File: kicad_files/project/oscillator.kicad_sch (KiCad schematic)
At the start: 3 parts, among them X1 TXM12M0004252DBCEO00T

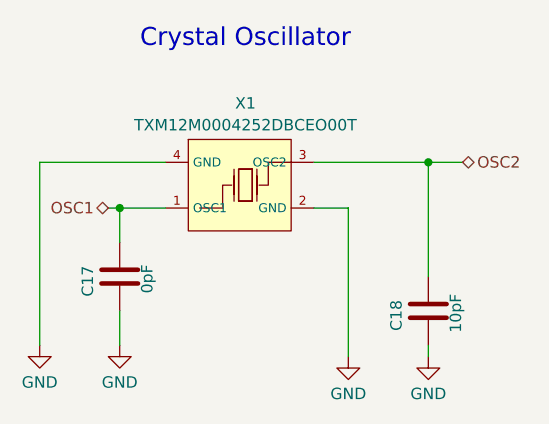
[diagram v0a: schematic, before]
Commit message: started with board layout, also added more stuff on the schematic
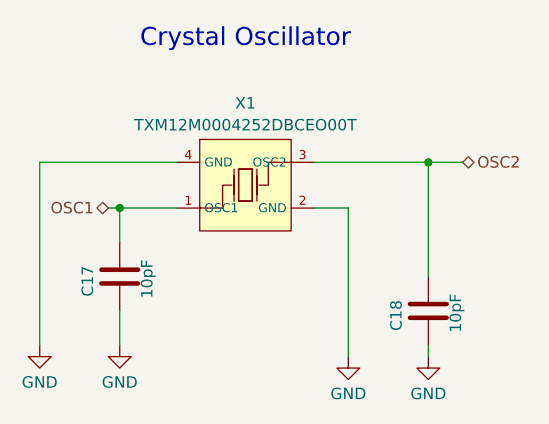
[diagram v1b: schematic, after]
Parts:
- C17: value 0pF -> 10pF
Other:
- moved on the sheet: X1
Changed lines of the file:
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@@
 	(wire
 		(pts
-			(xy 123.19 91.44) (xy 128.27 91.44)
+			(xy 123.19 91.44) (xy 129.54 91.44)
 		)
 		(stroke
@@
 	(wire
 		(pts
-			(xy 114.3 86.36) (xy 128.27 86.36)
+			(xy 114.3 86.36) (xy 129.54 86.36)
 		)
 		(stroke
@@
 		(dnp no)
 		(fields_autoplaced yes)
-		(property "Reference" "#PWR033"
+		(property "Reference" "#PWR044"
 			(at 123.19 113.03 0)
 			(effects
@@
 			(project "FABulous_board"
 				(path "/5664f05e-a3ef-4177-8026-c4580fa32c71/b4d9b251-031a-4875-8b01-0478a187070c/4c7542bb-a835-445d-b466-6e95b674eb44"
-					(reference "#PWR033")
+					(reference "#PWR044")
 					(unit 1)
 				)
@@
 		(on_board yes)
 		(dnp no)
-		(fields_autoplaced yes)
 		(property "Reference" "X1"
 			(at 137.16 79.8025 0)
@@
 		(dnp no)
 		(fields_autoplaced yes)
-		(property "Reference" "#PWR032"
+		(property "Reference" "#PWR043"
 			(at 114.3 113.03 0)
 			(effects
@@
 			(project "FABulous_board"
 				(path "/5664f05e-a3ef-4177-8026-c4580fa32c71/b4d9b251-031a-4875-8b01-0478a187070c/4c7542bb-a835-445d-b466-6e95b674eb44"
-					(reference "#PWR032")
+					(reference "#PWR043")
 					(unit 1)
 				)
@@
 		(dnp no)
 		(fields_autoplaced yes)
-		(property "Reference" "#PWR034"
+		(property "Reference" "#PWR045"
 			(at 148.59 114.3 0)
 			(effects
@@
 			(project "FABulous_board"
 				(path "/5664f05e-a3ef-4177-8026-c4580fa32c71/b4d9b251-031a-4875-8b01-0478a187070c/4c7542bb-a835-445d-b466-6e95b674eb44"
-					(reference "#PWR034")
+					(reference "#PWR045")
 					(unit 1)
 				)
@@
 		(dnp no)
 		(fields_autoplaced yes)
-		(property "Reference" "#PWR035"
+		(property "Reference" "#PWR046"
 			(at 157.48 114.3 0)
 			(effects
@@
 			(project "FABulous_board"
 				(path "/5664f05e-a3ef-4177-8026-c4580fa32c71/b4d9b251-031a-4875-8b01-0478a187070c/4c7542bb-a835-445d-b466-6e95b674eb44"
-					(reference "#PWR035")
+					(reference "#PWR046")
 					(unit 1)
 				)
@@
 			)
 		)
-		(property "Value" "0pF"
+		(property "Value" "10pF"
 			(at 126.238 99.314 90)
 			(effects
